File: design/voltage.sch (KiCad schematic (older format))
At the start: 12 parts

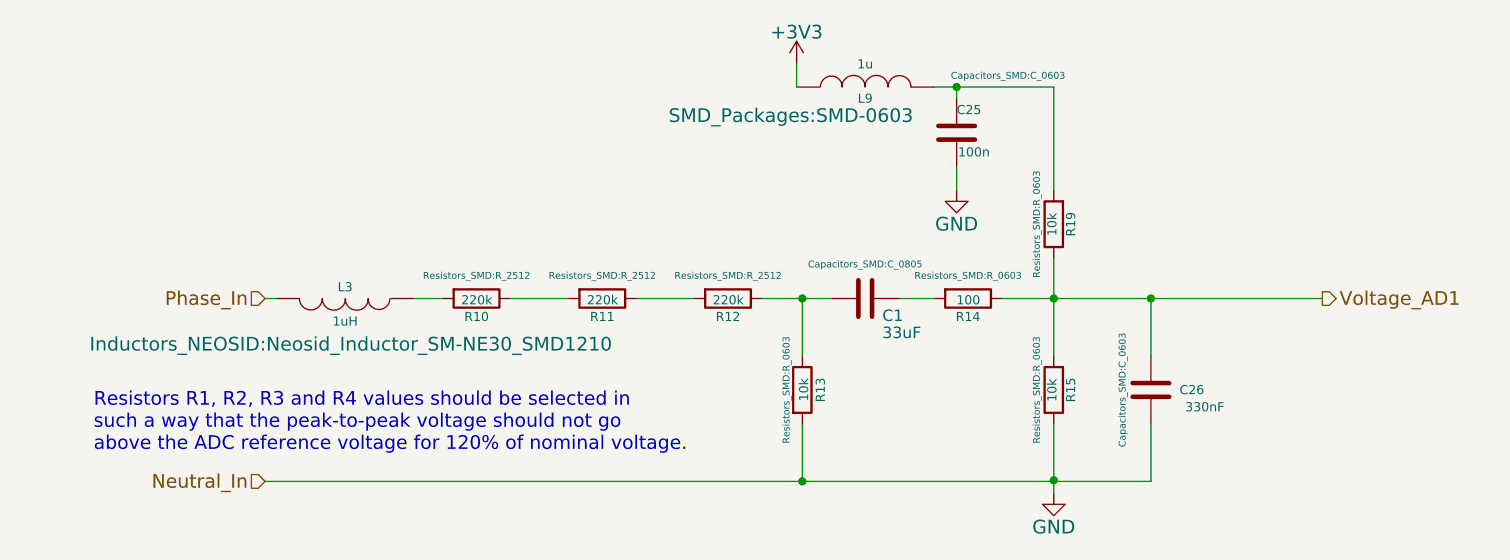
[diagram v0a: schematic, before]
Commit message: Moving to PIVI 2.0, added circuits for current clamps
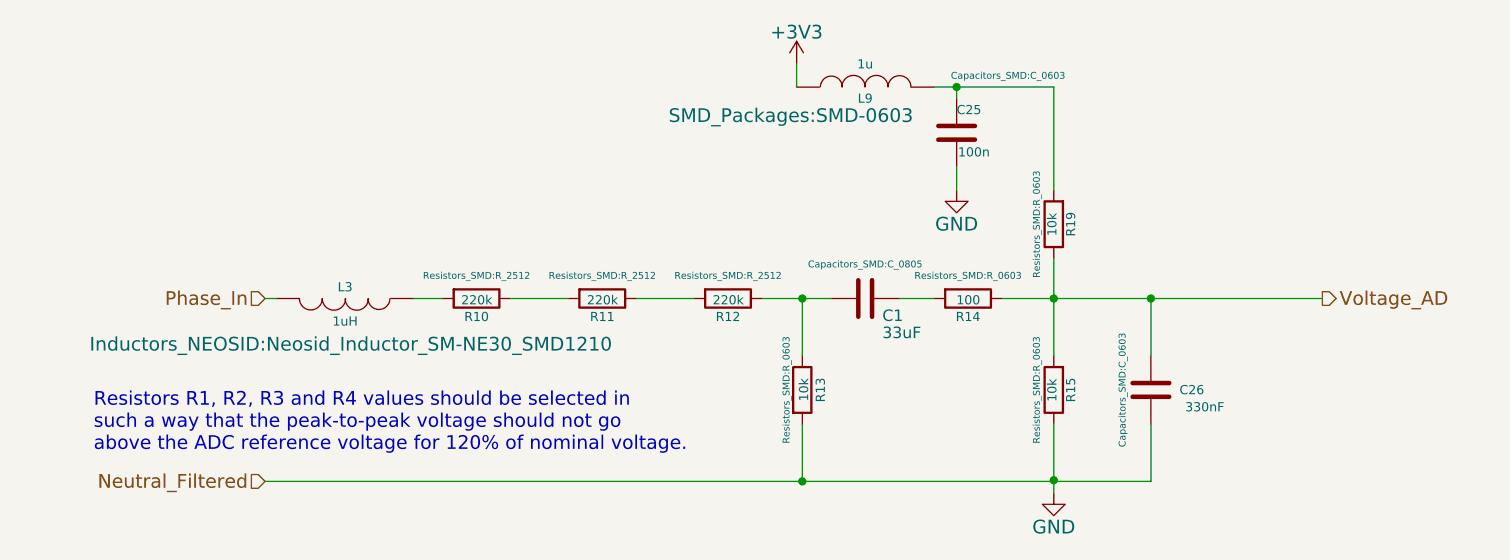
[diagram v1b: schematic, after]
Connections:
- net labels added: Neutral_Filtered, Voltage_AD
- net labels removed: Neutral_In, Voltage_AD1
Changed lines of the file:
@@
 $Descr A4 11693 8268
 encoding utf-8
-Sheet 5 14
+Sheet 12 18
 Title "PIVI"
-Date ""
-Rev "1.0"
+Date "Mon 27 Jul 2015"
+Rev "2.0"
 Comp "Copyright (C) LESS industries S.A. 2014,2015"
 Comment1 "Share alike attribution non-commercial 4.0"
@@
 $EndDescr
 Text HLabel 8460 3835 2    60   Output ~ 0
-Voltage_AD1
+Voltage_AD
 Text HLabel 3835 3835 0    60   Input ~ 0
 Phase_In
 Text HLabel 3835 4635 0    60   Input ~ 0
-Neutral_In
+Neutral_Filtered
 $Comp
 L R R13
@@
 AR Path="/548EAA5D/548E244E/5497B2D6" Ref="R53"  Part="1"
 AR Path="/548EAA5D/548E282E/5497B2D6" Ref="R63"  Part="1"
+AR Path="/548DF2C8/55B216B6/5497B2D6" Ref="R13"  Part="1"
 F 0 "R13" V 6265 4235 40  0000 C CNN
 F 1 "10k" V 6192 4236 40  0000 C CNN
@@
 AR Path="/548EAA5D/548E244E/5497B2DD" Ref="R54"  Part="1"
 AR Path="/548EAA5D/548E282E/5497B2DD" Ref="R64"  Part="1"
+AR Path="/548DF2C8/55B216B6/5497B2DD" Ref="R14"  Part="1"
 F 0 "R14" V 6990 3835 40  0000 C CNN
 F 1 "100" V 6917 3836 40  0000 C CNN
@@
 AR Path="/548EAA5D/548E244E/5497B2E4" Ref="C45"  Part="1"
 AR Path="/548EAA5D/548E282E/5497B2E4" Ref="C50"  Part="1"
+AR Path="/548DF2C8/55B216B6/5497B2E4" Ref="C25"  Part="1"
 F 0 "C25" H 6860 3210 40  0000 L CNN
 F 1 "100n" H 6866 3025 40  0000 L CNN
@@
 AR Path="/548EAA5D/548E244E/5497B2EB" Ref="C46"  Part="1"
 AR Path="/548EAA5D/548E282E/5497B2EB" Ref="C51"  Part="1"
+AR Path="/548DF2C8/55B216B6/5497B2EB" Ref="C26"  Part="1"
 F 0 "C26" H 7835 4235 40  0000 L CNN
 F 1 "330nF" H 7860 4160 40  0000 L CNN
@@
 AR Path="/548EAA5D/548E244E/5497B2FF" Ref="R55"  Part="1"
 AR Path="/548EAA5D/548E282E/5497B2FF" Ref="R65"  Part="1"
+AR Path="/548DF2C8/55B216B6/5497B2FF" Ref="R15"  Part="1"
 F 0 "R15" V 7210 4235 40  0000 C CNN
 F 1 "10k" V 7292 4236 40  0000 C CNN
@@
 AR Path="/548EAA5D/548E244E/548E33DD" Ref="R50"  Part="1"
 AR Path="/548EAA5D/548E282E/548E33DD" Ref="R60"  Part="1"
+AR Path="/548DF2C8/55B216B6/548E33DD" Ref="R10"  Part="1"
 F 0 "R10" V 4840 3835 40  0000 C CNN
 F 1 "220k" V 4767 3836 40  0000 C CNN
@@
 AR Path="/548EAA5D/548E244E/548E40C9" Ref="R59"  Part="1"
 AR Path="/548EAA5D/548E282E/548E40C9" Ref="R69"  Part="1"
+AR Path="/548DF2C8/55B216B6/548E40C9" Ref="R19"  Part="1"
 F 0 "R19" V 7210 3510 40  0000 C CNN
 F 1 "10k" V 7292 3511 40  0000 C CNN
@@
 AR Path="/548EAA5D/548E244E/548E4464" Ref="L7"  Part="1"
 AR Path="/548EAA5D/548E282E/548E4464" Ref="L8"  Part="1"
+AR Path="/548DF2C8/55B216B6/548E4464" Ref="L3"  Part="1"
 F 0 "L3" V 4135 3835 40  0000 C CNN
 F 1 "1uH" V 4285 3835 40  0000 C CNN
@@
 AR Path="/548EAA5D/548E244E/548DF4C0" Ref="R51"  Part="1"
 AR Path="/548EAA5D/548E282E/548DF4C0" Ref="R61"  Part="1"
+AR Path="/548DF2C8/55B216B6/548DF4C0" Ref="R11"  Part="1"
 F 0 "R11" V 5390 3835 40  0000 C CNN
 F 1 "220k" V 5317 3836 40  0000 C CNN
@@
 AR Path="/548EAA5D/548E244E/548DF506" Ref="R52"  Part="1"
 AR Path="/548EAA5D/548E282E/548DF506" Ref="R62"  Part="1"
+AR Path="/548DF2C8/55B216B6/548DF506" Ref="R12"  Part="1"
 F 0 "R12" V 5940 3835 40  0000 C CNN
 F 1 "220k" V 5867 3836 40  0000 C CNN
@@
 AR Path="/548EAA5D/548E244E/54BDE7C8" Ref="L13"  Part="1"
 AR Path="/548EAA5D/548E282E/54BDE7C8" Ref="L14"  Part="1"
+AR Path="/548DF2C8/55B216B6/54BDE7C8" Ref="L9"  Part="1"
 F 0 "L9" V 6410 2910 40  0000 C CNN
 F 1 "1u" V 6560 2910 40  0000 C CNN
@@
 AR Path="/548EAA5D/548E244E/54BE015B" Ref="#PWR071"  Part="1"
 AR Path="/548EAA5D/548E282E/54BE015B" Ref="#PWR079"  Part="1"
-F 0 "#PWR034" H 6160 2660 60  0001 C CNN
+AR Path="/548DF2C8/55B216B6/54BE015B" Ref="#PWR050"  Part="1"
+F 0 "#PWR050" H 6160 2660 60  0001 C CNN
 F 1 "+3V3" H 6160 2950 60  0000 C CNN
 F 2 "" H 6160 2810 60  0000 C CNN
@@
 AR Path="/548EAA5D/548E244E/54C00611" Ref="#PWR072"  Part="1"
 AR Path="/548EAA5D/548E282E/54C00611" Ref="#PWR080"  Part="1"
-F 0 "#PWR035" H 6860 3110 60  0001 C CNN
+AR Path="/548DF2C8/55B216B6/54C00611" Ref="#PWR051"  Part="1"
+F 0 "#PWR051" H 6860 3110 60  0001 C CNN
 F 1 "GND" H 6860 3210 60  0000 C CNN
 F 2 "" H 6860 3360 60  0000 C CNN
@@
 AR Path="/548EAA5D/548E244E/54C006EB" Ref="#PWR073"  Part="1"
 AR Path="/548EAA5D/548E282E/54C006EB" Ref="#PWR081"  Part="1"
-F 0 "#PWR036" H 7285 4435 60  0001 C CNN
+AR Path="/548DF2C8/55B216B6/54C006EB" Ref="#PWR052"  Part="1"
+F 0 "#PWR052" H 7285 4435 60  0001 C CNN
 F 1 "GND" H 7285 4535 60  0000 C CNN
 F 2 "" H 7285 4685 60  0000 C CNN
@@
 AR Path="/548EAA5D/548E244E/54C1942B" Ref="C5"  Part="1"
 AR Path="/548EAA5D/548E282E/54C1942B" Ref="C6"  Part="1"
+AR Path="/548DF2C8/55B216B6/54C1942B" Ref="C1"  Part="1"
 F 0 "C1" V 6535 3910 50  0000 L CNN
 F 1 "33uF" V 6610 3910 50  0000 L CNN

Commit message: Fixing connection errors
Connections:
- net labels added: Phase_Line
- net labels removed: Phase_In
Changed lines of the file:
@@
 Text HLabel 8460 3835 2    60   Output ~ 0
 Voltage_AD
-Text HLabel 3835 3835 0    60   Input ~ 0
-Phase_In
+Text HLabel 3745 3835 0    60   Input ~ 0
+Phase_Line
 Text HLabel 3835 4635 0    60   Input ~ 0
 Neutral_Filtered
@@
 	-1   0    0    1
 $EndComp
-$Comp
-L INDUCTOR L3
-U 1 1 548E4464
-P 4185 3835
-AR Path="/548DF2C8/548E1940/548E4464" Ref="L3"  Part="1"
-AR Path="/548DF2C8/548E244E/548E4464" Ref="L4"  Part="1"
-AR Path="/548DF2C8/548E282E/548E4464" Ref="L5"  Part="1"
-AR Path="/548EAA5D/548E1940/548E4464" Ref="L6"  Part="1"
-AR Path="/548EAA5D/548E244E/548E4464" Ref="L7"  Part="1"
-AR Path="/548EAA5D/548E282E/548E4464" Ref="L8"  Part="1"
-AR Path="/548DF2C8/55B216B6/548E4464" Ref="L3"  Part="1"
-F 0 "L3" V 4135 3835 40  0000 C CNN
-F 1 "1uH" V 4285 3835 40  0000 C CNN
-F 2 "Inductors_NEOSID:Neosid_Inductor_SM-NE30_SMD1210" V 4385 3860 60  0000 C CNN
-F 3 "" H 4185 3835 60  0000 C CNN
-	1    4185 3835
-	0    1    1    0
-$EndComp
 Text Notes 3085 4510 0    60   ~ 0
 Resistors R1, R2, R3 and R4 values should be selected in \nsuch a way that the peak-to-peak voltage should not go\nabove the ADC reference voltage for 120% of nominal voltage.
@@
 AR Path="/548EAA5D/548E244E/54BE015B" Ref="#PWR071"  Part="1"
 AR Path="/548EAA5D/548E282E/54BE015B" Ref="#PWR079"  Part="1"
-AR Path="/548DF2C8/55B216B6/54BE015B" Ref="#PWR050"  Part="1"
-F 0 "#PWR050" H 6160 2660 60  0001 C CNN
+AR Path="/548DF2C8/55B216B6/54BE015B" Ref="#PWR051"  Part="1"
+F 0 "#PWR051" H 6160 2660 60  0001 C CNN
 F 1 "+3V3" H 6160 2950 60  0000 C CNN
 F 2 "" H 6160 2810 60  0000 C CNN
@@
 AR Path="/548EAA5D/548E244E/54C00611" Ref="#PWR072"  Part="1"
 AR Path="/548EAA5D/548E282E/54C00611" Ref="#PWR080"  Part="1"
-AR Path="/548DF2C8/55B216B6/54C00611" Ref="#PWR051"  Part="1"
-F 0 "#PWR051" H 6860 3110 60  0001 C CNN
+AR Path="/548DF2C8/55B216B6/54C00611" Ref="#PWR052"  Part="1"
+F 0 "#PWR052" H 6860 3110 60  0001 C CNN
 F 1 "GND" H 6860 3210 60  0000 C CNN
 F 2 "" H 6860 3360 60  0000 C CNN
@@
 AR Path="/548EAA5D/548E244E/54C006EB" Ref="#PWR073"  Part="1"
 AR Path="/548EAA5D/548E282E/54C006EB" Ref="#PWR081"  Part="1"
-AR Path="/548DF2C8/55B216B6/54C006EB" Ref="#PWR052"  Part="1"
-F 0 "#PWR052" H 7285 4435 60  0001 C CNN
+AR Path="/548DF2C8/55B216B6/54C006EB" Ref="#PWR053"  Part="1"
+F 0 "#PWR053" H 7285 4435 60  0001 C CNN
 F 1 "GND" H 7285 4535 60  0000 C CNN
 F 2 "" H 7285 4685 60  0000 C CNN
@@
 Connection ~ 6185 4635
 Wire Wire Line
-	3835 3835 3885 3835
-Wire Wire Line
 	7285 3660 7285 4085
 Wire Wire Line
@@
 	6160 2910 6160 2810
 Wire Wire Line
-	4485 3835 4610 3835
+	4475 3835 4610 3835
 Wire Wire Line
 	4910 3835 5160 3835
@@
 Connection ~ 7285 3835
 Connection ~ 7710 3835
+$Comp
+L INDUCTOR L3
+U 1 1 548E4464
+P 4175 3835
+AR Path="/548DF2C8/548E1940/548E4464" Ref="L3"  Part="1"
+AR Path="/548DF2C8/548E244E/548E4464" Ref="L4"  Part="1"
+AR Path="/548DF2C8/548E282E/548E4464" Ref="L5"  Part="1"
+AR Path="/548EAA5D/548E1940/548E4464" Ref="L6"  Part="1"
+AR Path="/548EAA5D/548E244E/548E4464" Ref="L7"  Part="1"
+AR Path="/548EAA5D/548E282E/548E4464" Ref="L8"  Part="1"
+AR Path="/548DF2C8/55B216B6/548E4464" Ref="L3"  Part="1"
+F 0 "L3" V 4125 3835 40  0000 C CNN
+F 1 "1uH" V 4275 3835 40  0000 C CNN
+F 2 "Inductors_NEOSID:Neosid_Inductor_SM-NE30_SMD1210" V 4375 3860 60  0000 C CNN
+F 3 "" H 4175 3835 60  0000 C CNN
+	1    4175 3835
+	0    1    1    0
+$EndComp
+Wire Wire Line
+	3745 3835 3875 3835
 $EndSCHEMATC

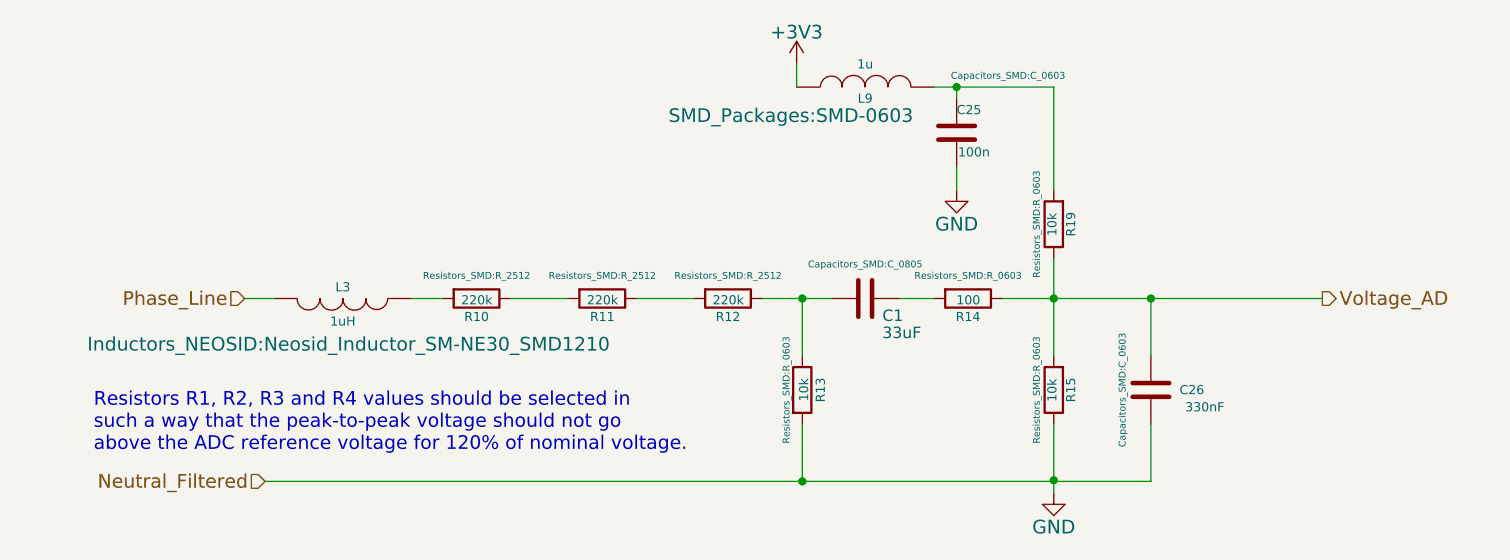
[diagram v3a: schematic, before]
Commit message: Edito conexiones pinza, agregado debub uart, agregado tension referencia
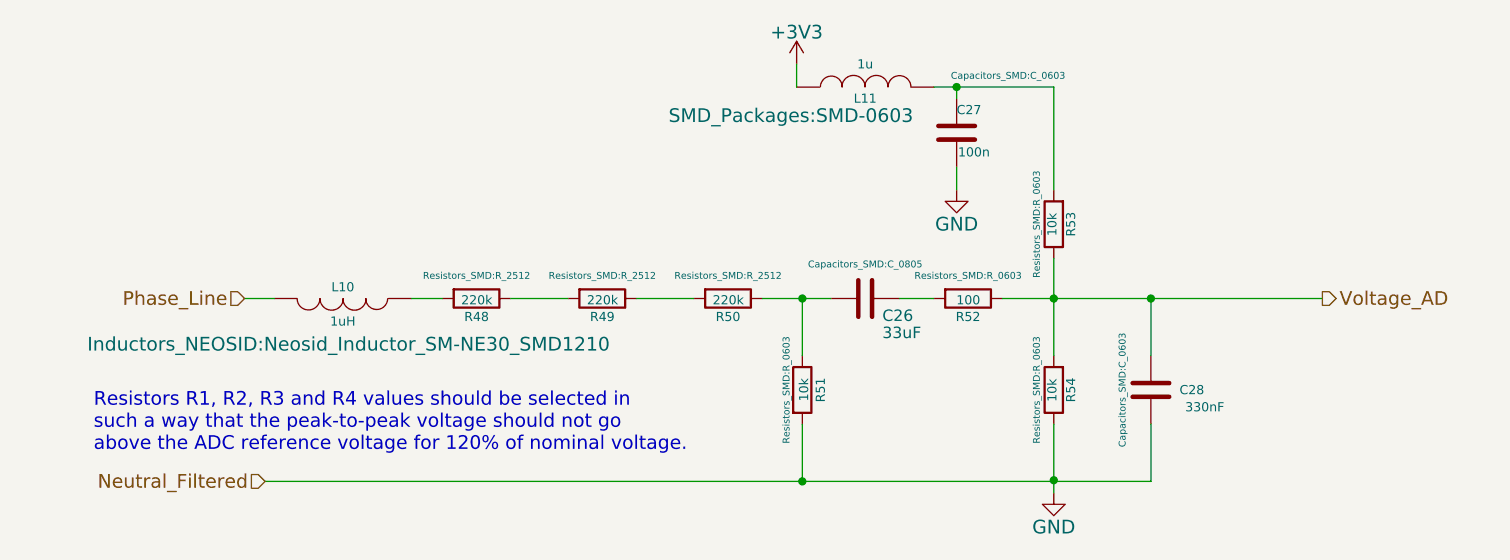
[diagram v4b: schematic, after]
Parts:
- renumbered C1 to C14, C25 to C15, C26 to C16, L3 to L6, L9 to L7, R10 to R16, R11 to R17, R12 to R18, R13 to R19, R14 to R20, R19 to R21, R15 to R22
